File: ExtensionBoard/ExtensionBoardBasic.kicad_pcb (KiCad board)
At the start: 2 copper layers, 65.2 x 110.3 mm, 23 parts, among them U1 KH-2.54FH-1X15P-H8.5, U1 Unidirectional 5.5V 6V SOT-14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, U2 C193852, U2 PM2.54-2*15, U3 KH-2.54PH180-3X15P-L11.5

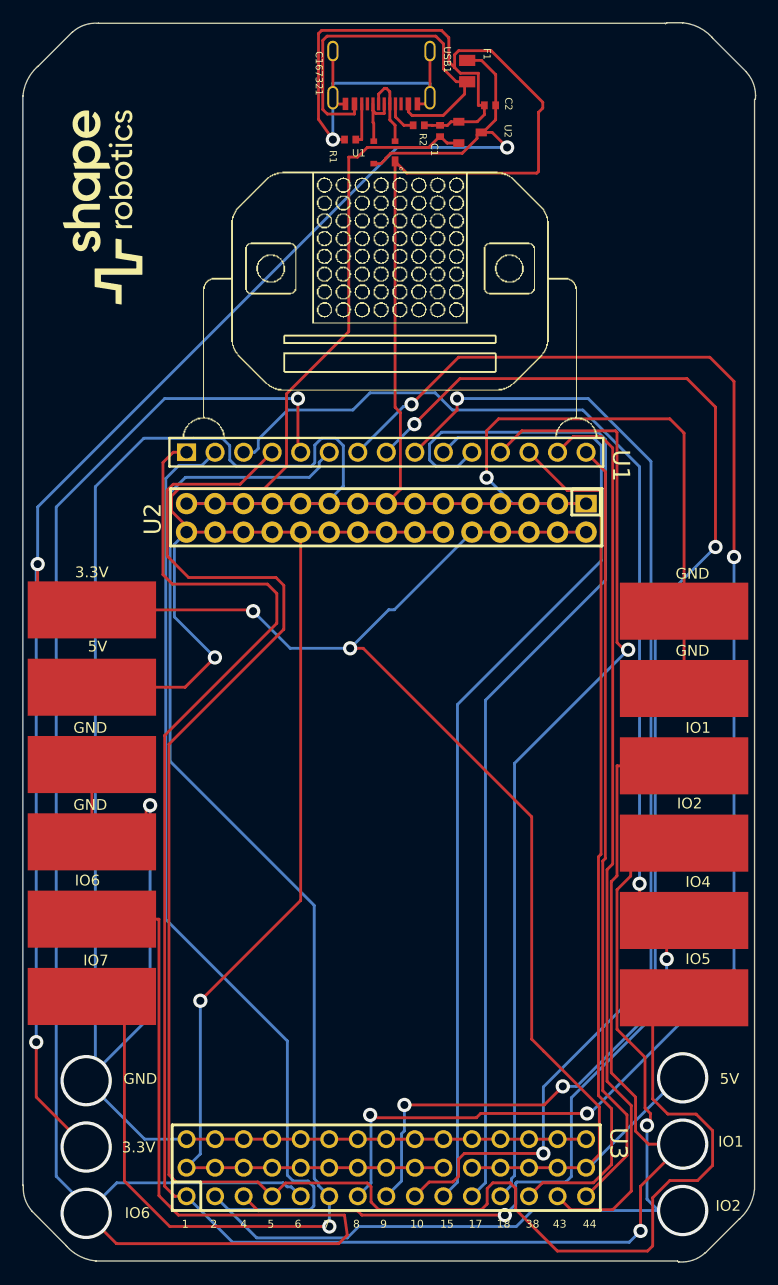
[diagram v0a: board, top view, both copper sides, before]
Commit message: extension board imported
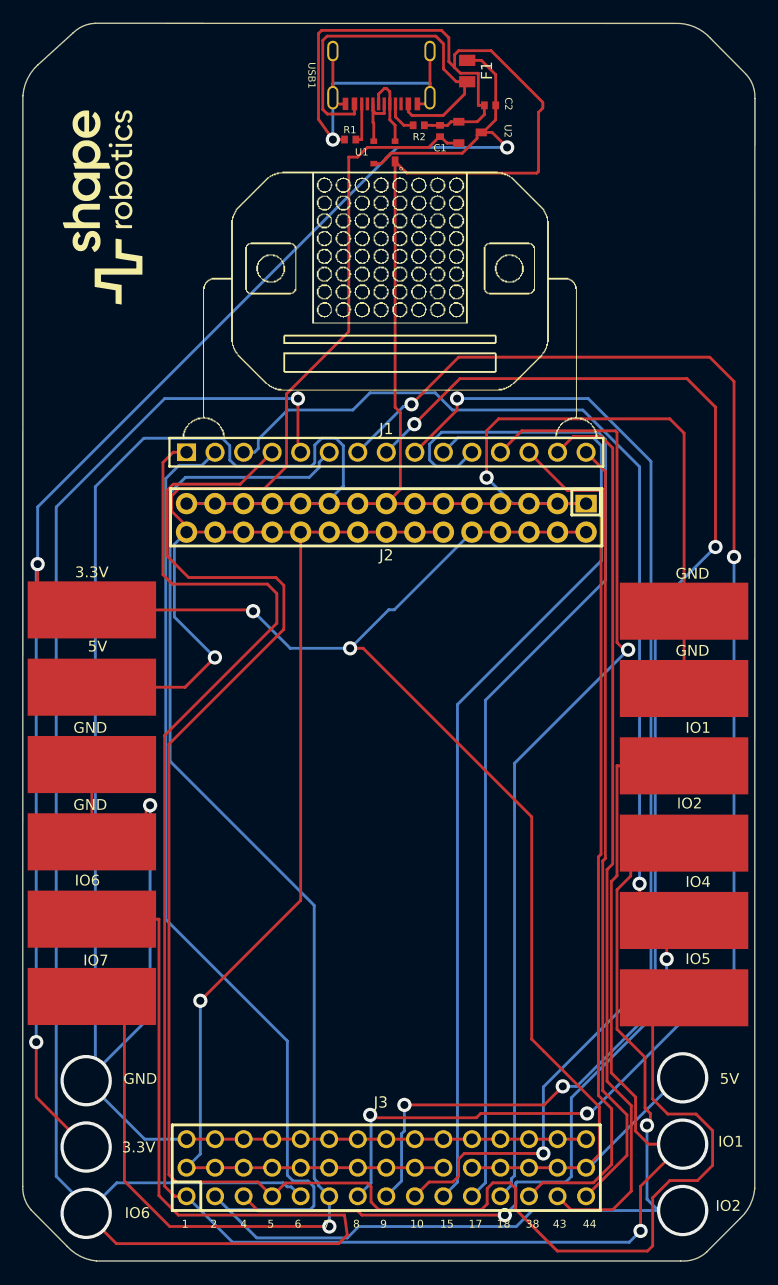
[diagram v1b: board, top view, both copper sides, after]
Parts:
- removed the U1 at (148.2, 88.1)
- removed the U2 at (148.2, 93.9)
- removed U3: KH-2.54PH180-3X15P-L11.5, HDR-TH_15P-P2.54-V-M-R3-C15-S2.54:HDR-TH_15P-P2.54-V-M-R3-C15-S2.54
- added J1: KH-2.54FH-1X15P-H8.5, FableFootPrintLibrary:HDR-TH_15P-P2.54-V-F, F.Cu at (148.2, 88.1)
- added J2: PM2.54-2*15, FableFootPrintLibrary:HDR-TH_30P-P2.54-V-F-R2-C15-S2.54, F.Cu at (148.2, 93.9)
- added J3: KH-2.54PH180-3X15P-L11.5, FableFootPrintLibrary:HDR-TH_15P-P2.54-V-M-R3-C15-S2.54, F.Cu at (148.2, 151.8)
- F1: footprint Hub 2.0:0805 -> FableFootPrintLibrary:0805
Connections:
- net NetR1_2 renamed Net-(USB1-CC2)
- net NetR2_2 renamed Net-(USB1-CC1)
- net fuse renamed //fuse
- ? pad 3: NetU1_1 -> //IO01
- ? pad 3: NetU1_2 -> //IO02
- ? pad 3: NetU1_4 -> //IO5
- ? pad 3: NetU1_5 -> //IO6
- ? pad 3: NetU1_3 -> //IO4
- ? pad 3: NetU1_6 -> //IO7
- USB1 pad A8: (no net) -> unconnected-(USB1-SBU1-PadA8)
- USB1 pad B8: (no net) -> unconnected-(USB1-SBU2-PadB8)
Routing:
- net NetU1_5: track 189.3 -> 0.00 mm, vias 2 -> 0
- net //IO6: track 0.00 -> 189.3 mm, vias 0 -> 2
- net NetU1_1: track 178.5 -> 0.00 mm, vias 2 -> 0
- net //IO01: track 0.00 -> 178.5 mm, vias 0 -> 2
- net NetU1_4: track 168.7 -> 0.00 mm
- net NetU1_2: track 168.0 -> 0.00 mm, vias 2 -> 0
- net //IO02: track 0.00 -> 168.0 mm, vias 0 -> 2
- net //IO5: track 0.00 -> 165.9 mm
- net NetU1_3: track 144.7 -> 0.00 mm, vias 3 -> 0
- net //IO4: track 0.00 -> 144.7 mm, vias 0 -> 3
- net NetU1_7: track 135.0 -> 0.00 mm, vias 4 -> 0
- net //IO8: track 0.00 -> 135.0 mm, vias 0 -> 4
- net //IO7: track 0.00 -> 126.3 mm, vias 0 -> 1
- net NetU1_6: track 126.3 -> 0.00 mm, vias 1 -> 0
- net NetU1_8: track 123.2 -> 0.00 mm, vias 4 -> 0
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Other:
- board size 65.2 x 110.3 mm -> 65.2 x 110.2 mm
- copper layers 2 -> 4
